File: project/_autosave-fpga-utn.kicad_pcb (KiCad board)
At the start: 2 copper layers, 76 parts, among them J1 USB_C_Receptacle_USB2.0_16P, U1 LD1117S33TR_SOT223, U2 LD1117S12TR_SOT223, U3 USBLC6-2SC6, U4 FT2232HL, U5 M93C66, U6 ICE40HX4K-TQ144, U7 W25X40CLSN, X1 ECS-3225MV-120-BN-TR

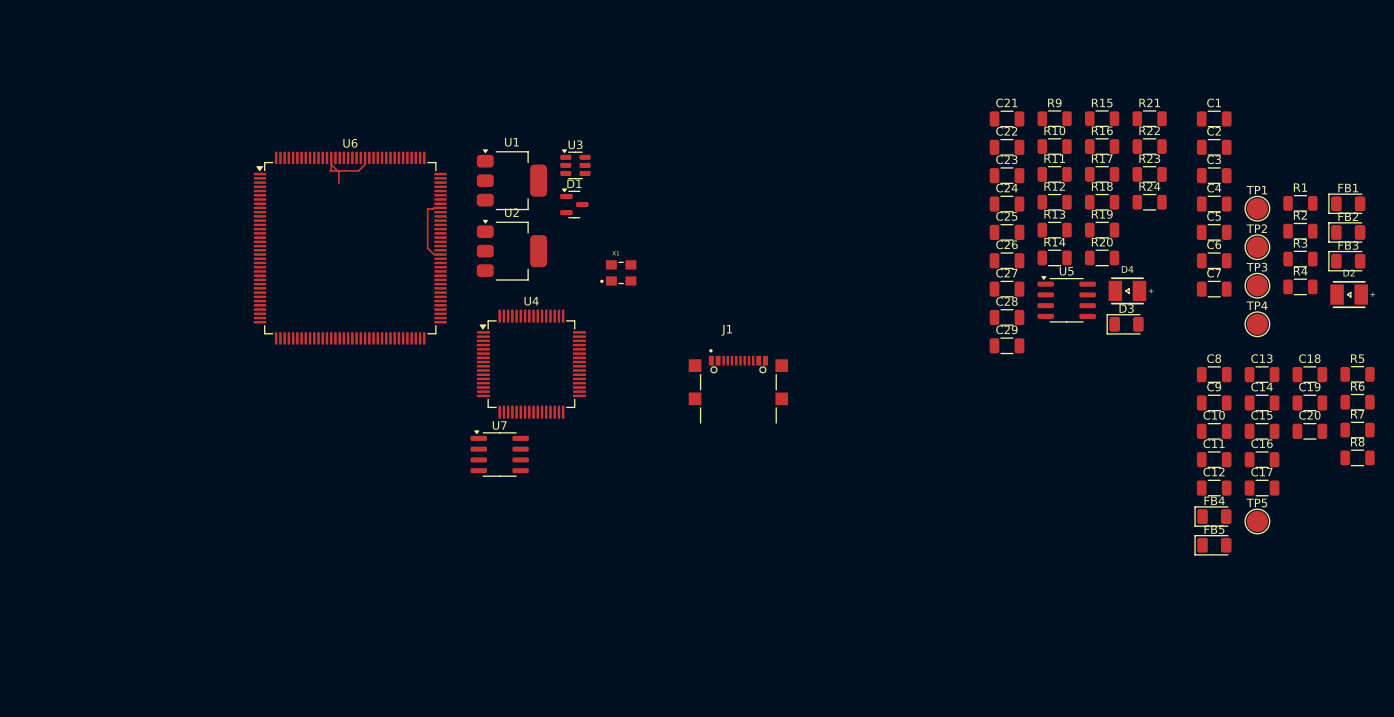
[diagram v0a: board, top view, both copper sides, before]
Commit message: Inicio de la PCB y conexion del PLL
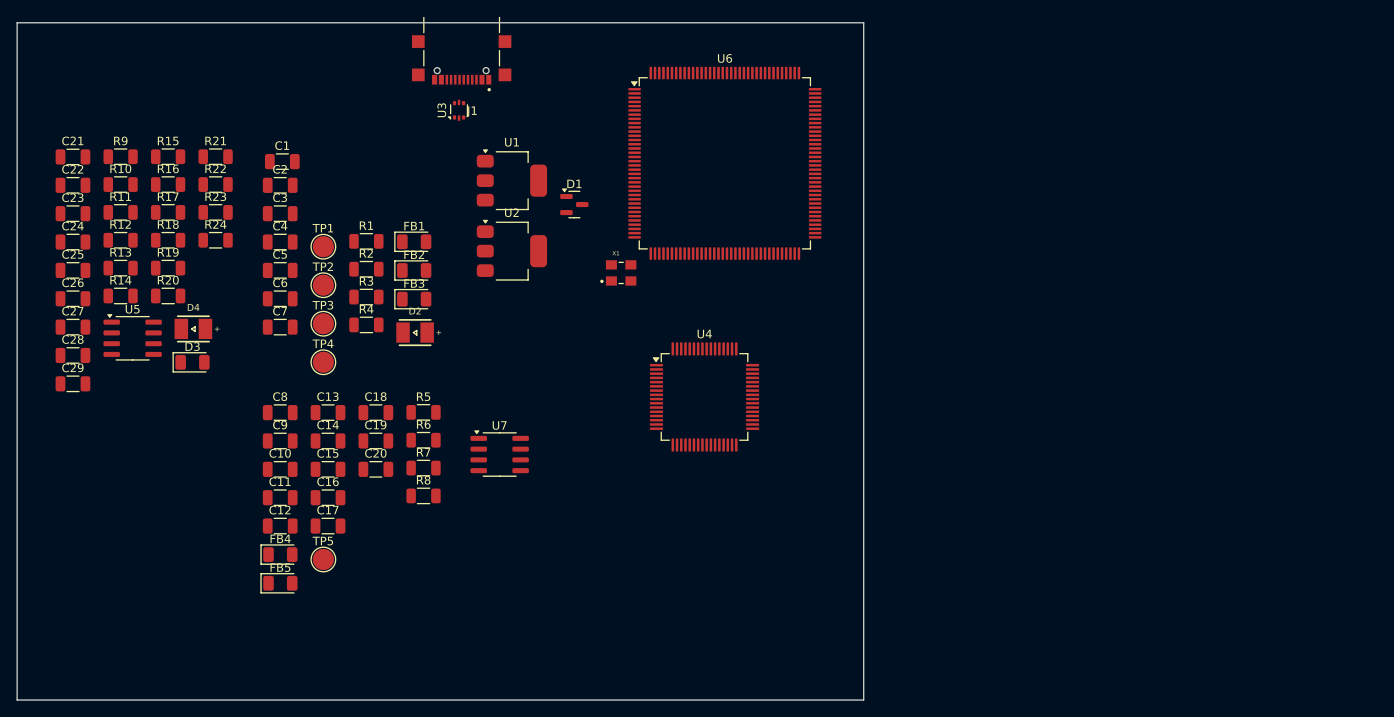
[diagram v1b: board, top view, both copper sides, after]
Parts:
- U3: footprint Package_TO_SOT_SMD:SOT-23-6 -> Package_TO_SOT_SMD:SOT-666
- moved C12 110.4 mm to (131.1, 109.5)
- moved C14 110.4 mm to (136.7, 99.4)
- moved C17 110.4 mm to (136.7, 109.5)
- moved C19 110.4 mm to (142.4, 99.4)
- moved C2 110.4 mm to (131.1, 69.2)
- moved C22 110.4 mm to (106.6, 69.2)
- moved C24 110.4 mm to (106.6, 75.9)
- moved C27 110.4 mm to (106.6, 86.0)
- moved C29 110.4 mm to (106.6, 92.7)
- moved C4 110.4 mm to (131.1, 75.9)
- moved C7 110.4 mm to (131.1, 86.0)
- moved C9 110.4 mm to (131.1, 99.4)
- moved D4 110.4 mm to (120.8, 86.2)
- moved FB1 110.4 mm to (146.9, 75.9)
- moved FB2 110.4 mm to (146.9, 79.3)
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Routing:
- net Net-(U6A-VCCIO_0-Pad123): track 10.2 -> 0.00 mm
- net Net-(U6B-VCCIO_1-Pad100): track 8.02 -> 0.00 mm
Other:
- board outline added: 100 x 80 mm
